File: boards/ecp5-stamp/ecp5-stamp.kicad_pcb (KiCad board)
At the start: 4 copper layers, 25 x 25 mm, 47 parts, among them J1 West, J2 South, J3 East, J4 North, J5 JTAG, SW1 ~RESET, SW2 ~USER, U1 W25Q128JVS, U2 MCP73831-2-OT, U3 ECP5UM_25_CSFBGA285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

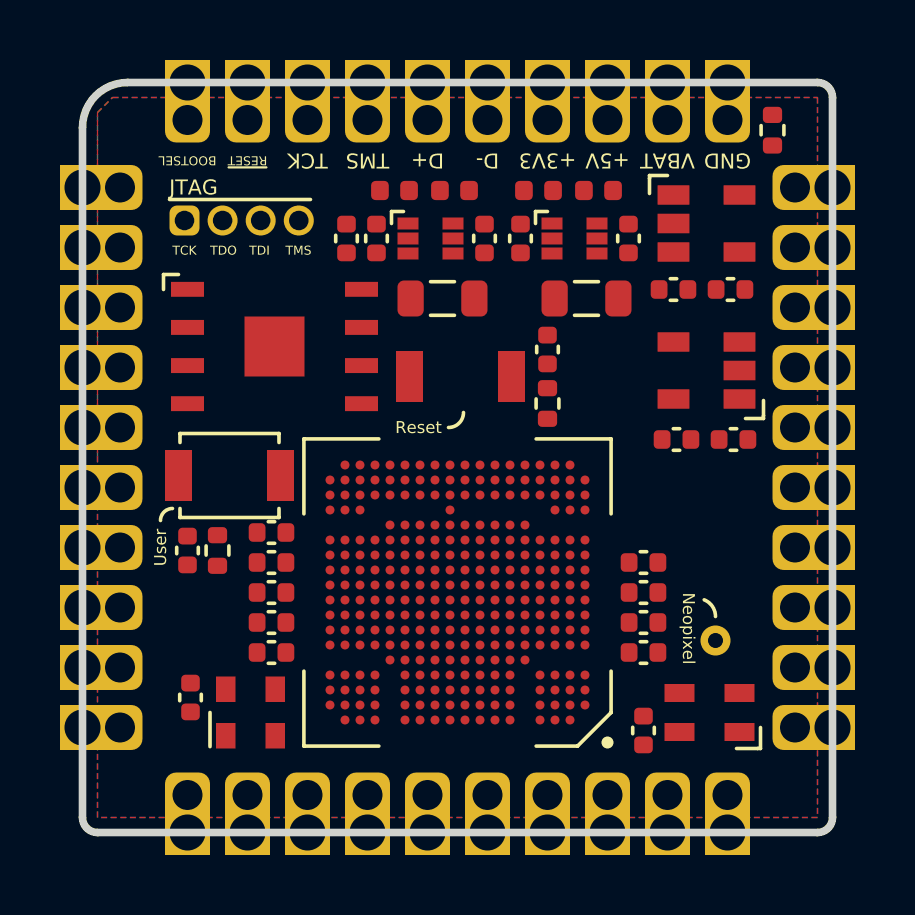
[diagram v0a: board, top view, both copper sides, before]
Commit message: Finished routing.
* Not sure what to do with BOOTSEL.
* Not sure if JTAG header is adequite.
* Not sure if should route dpairs equal length/together.
* etc.
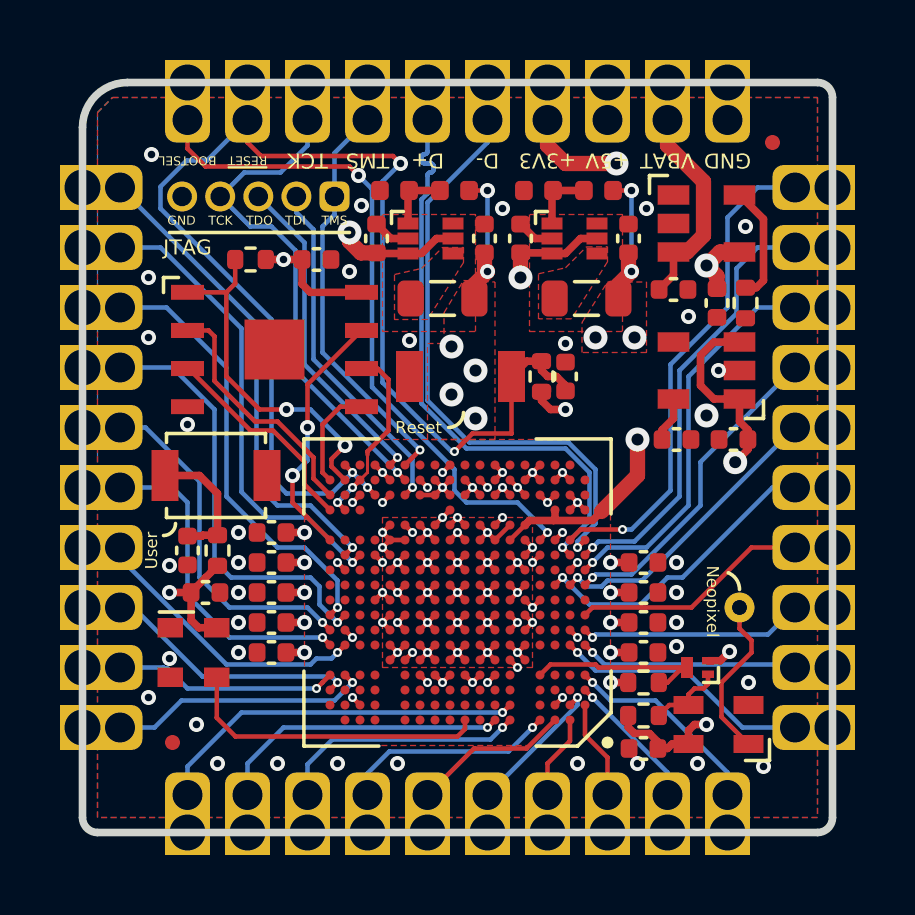
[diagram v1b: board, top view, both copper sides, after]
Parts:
- added FID1: Fiducial, Fiducial:Fiducial_0.5mm_Mask1mm, F.Cu at (25.0, 44.0)
- added FID2: Fiducial, Fiducial:Fiducial_0.5mm_Mask1mm, F.Cu at (45.0, 24.0)
- added Q1: DMN21D2UFB-7B, Package_DFN_QFN:Diodes_DFN1006-3, F.Cu at (42.5, 41.5)
- added R10: 4k7, Resistor_SMD:R_0402_1005Metric, F.Cu at (40.7, 43.1)
- added R8: 4k7, Resistor_SMD:R_0402_1005Metric, F.Cu at (27.6, 27.9)
- added R9: 4k7, Resistor_SMD:R_0402_1005Metric, F.Cu at (40.7, 42.0)
- J5: footprint Connector_PinHeader_1.27mm:PinHeader_1x04_P1.27mm_Vertical -> Connector_PinHeader_1.27mm:PinHeader_1x05_P1.27mm_Vertical
- moved R7 5.83 mm to (44.1, 29.4), turned to 270 degrees
- moved J5 5.06 mm to (30.4, 25.8), turned to 270 degrees
- moved C18 3.54 mm to (26.1, 39.0), turned to 0 degrees
- moved U4 2.76 mm to (25.7, 41.0), turned to 270 degrees
- moved TP1 1.36 mm to (43.9, 39.5)
- moved C17 1.22 mm to (29.8, 27.9), turned to 0 degrees
- moved C1 1.08 mm to (38.1, 31.8)
- moved C3 1.00 mm to (40.7, 39.0)
- moved C4 1.00 mm to (28.3, 39.0)
- moved C5 1.00 mm to (28.3, 40.0)
- moved C9 1.00 mm to (40.7, 40.0)
- moved R1 0.92 mm to (37.3, 31.8)
- moved C20 0.64 mm to (43.1, 29.4), turned to 270 degrees
- moved C21 0.60 mm to (40.7, 44.2), turned to 180 degrees
- moved D1 0.50 mm to (43.2, 43.4)
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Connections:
- net Net-(L1-Pad1) renamed /SW_1V1
- net Net-(L2-Pad1) renamed /SW_3V3
- C15 pad 1: +1V2 -> +1V1
- C3 pad 1: +1V2 -> +1V1
- C4 pad 1: +1V2 -> +1V1
- J5 pad 1: /JTAG_TCK -> /JTAG_TMS
- J5 pad 2: /JTAG_TDO -> /JTAG_TDI
- J5 pad 3: /JTAG_TDI -> /JTAG_TDO
- J5 pad 4: /JTAG_TMS -> /JTAG_TCK
- L1 pad 2: +1V2 -> +1V1
- R2 pad 1: +1V2 -> +1V1
- U3 pad A2: Net-(U3-PadA2) -> /GPIO_16
- U3 pad A3: Net-(U3-PadA3) -> /GPIO_14
- U3 pad A4: Net-(U3-PadA4) -> /GPIO_13
- U3 pad A6: Net-(U3-PadA6) -> /GPIO_12
- U3 pad A7: Net-(U3-PadA7) -> /GPIO_11
- U3 pad A9: Net-(U3-PadA9) -> /REF_CLK
- U3 pad B1: Net-(U3-PadB1) -> /GPIO_17
- U3 pad B2: Net-(U3-PadB2) -> /GPIO_15
- U3 pad B6: Net-(U3-PadB6) -> /GPIO_10
- U3 pad C1: Net-(U3-PadC1) -> /GPIO_18
- U3 pad C18: Net-(U3-PadC18) -> /GPIO_07
- U3 pad D1: Net-(U3-PadD1) -> /GPIO_19
- U3 pad D10: +1V2 -> +1V1
- U3 pad D11: +1V2 -> +1V1
- U3 pad D17: Net-(U3-PadD17) -> /GPIO_09
- U3 pad D18: Net-(U3-PadD18) -> /GPIO_08
- U3 pad D4: Net-(U3-PadD4) -> /NP_SDI_LV
- U3 pad D8: +1V2 -> +1V1
- U3 pad D9: +1V2 -> +1V1
- U3 pad F1: Net-(U3-PadF1) -> /GPIO_21
- U3 pad F17: Net-(U3-PadF17) -> /GPIO_06
- U3 pad F18: Net-(U3-PadF18) -> /GPIO_05
- U3 pad F2: Net-(U3-PadF2) -> /GPIO_20
- U3 pad G1: Net-(U3-PadG1) -> /GPIO_22
- U3 pad G18: Net-(U3-PadG18) -> /GPIO_04
- U3 pad H1: Net-(U3-PadH1) -> /GPIO_23
- U3 pad H17: Net-(U3-PadH17) -> /GPIO_03
- U3 pad H18: Net-(U3-PadH18) -> /GPIO_02
- U3 pad J14: +1V2 -> +1V1
- U3 pad J15: +1V2 -> +1V1
- U3 pad J4: +1V2 -> +1V1
- U3 pad J5: +1V2 -> +1V1
- U3 pad K1: Net-(U3-PadK1) -> /GPIO_26
- U3 pad K2: Net-(U3-PadK2) -> /GPIO_25
- U3 pad K3: Net-(U3-PadK3) -> /GPIO_24
- U3 pad L1: Net-(U3-PadL1) -> /GPIO_27
- U3 pad M1: Net-(U3-PadM1) -> /GPIO_28
- U3 pad M15: +1V2 -> +1V1
- U3 pad M16: Net-(U3-PadM16) -> /GPIO_01
- U3 pad M17: Net-(U3-PadM17) -> /GPIO_00
- U3 pad M2: Net-(U3-PadM2) -> /USB_D+
- U3 pad M4: +1V2 -> +1V1
- U3 pad N1: Net-(U3-PadN1) -> /USB_D-
- U3 pad N18: Net-(U3-PadN18) -> /FLASH_IO3
- U3 pad N2: Net-(U3-PadN2) -> /GPIO_29
- U3 pad N4: Net-(U3-PadN4) -> /BOOTSEL
- U3 pad P10: Net-(U3-PadP10) -> +1V1
- U3 pad P11: +1V2 -> +1V1
- U3 pad P7: +1V2 -> +1V1
- U3 pad P9: +1V2 -> +1V1
- U3 pad R10: Net-(U3-PadP10) -> +1V1
- U3 pad R17: Net-(U3-PadR17) -> /FLASH_SCK
- U3 pad R18: Net-(U3-PadR18) -> /FLASH_IO2
- U3 pad T14: Net-(U3-PadT14) -> +3V3
- U3 pad T15: Net-(U3-PadT15) -> /~RESET
- U3 pad T18: Net-(U3-PadT18) -> /FLASH_IO1
- U3 pad T5: Net-(U3-PadT5) -> +1V1
- U3 pad U12: Net-(U3-PadU12) -> +1V1
- U3 pad U14: Net-(U3-PadU14) -> GND
- U3 pad U16: Net-(U3-PadU16) -> /FLASH_SCK
- U3 pad U17: Net-(U3-PadU17) -> /FLASH_CS
- U3 pad U18: Net-(U3-PadU18) -> /FLASH_IO0
- U3 pad U6: Net-(U3-PadU6) -> +1V1
- U3 pad U8: Net-(U3-PadU8) -> +1V1
- U3 pad V15: Net-(U3-PadV15) -> GND
- U3 pad V17: Net-(U3-PadV17) -> /~RESET
- U4 pad 3: /OSC_12MHz -> /REF_CLK
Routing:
- net +5V: track 0.00 -> 54.2 mm, vias 0 -> 4
- net /~RESET: track 0.00 -> 43.5 mm, vias 0 -> 4
- net GND: track 0.00 -> 42.3 mm, vias 0 -> 76
- net +3V3: track 0.00 -> 41.1 mm, vias 0 -> 26
- net +2V5: track 0.00 -> 36.0 mm, vias 0 -> 4
- net /BOOTSEL: track 0.00 -> 22.9 mm, vias 0 -> 2
- net /USB_D-: track 0.00 -> 19.9 mm, vias 0 -> 1
- net /USB_D+: track 0.00 -> 19.8 mm, vias 0 -> 1
- net +1V1: track 0.00 -> 17.9 mm, vias 0 -> 20
- net /JTAG_TCK: track 0.00 -> 16.9 mm, vias 0 -> 1
- net /GPIO_29: track 0.00 -> 16.6 mm, vias 0 -> 1
- net /GPIO_00: track 0.00 -> 16.2 mm, vias 0 -> 1
- net /GPIO_02: track 0.00 -> 15.8 mm, vias 0 -> 1
- net /GPIO_01: track 0.00 -> 15.6 mm, vias 0 -> 1
- net /GPIO_28: track 0.00 -> 14.6 mm, vias 0 -> 1
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- added copper zone on F.Cu, net +1V1
- added copper zone on In1.Cu, net +1V1
- added copper zone on F.Cu, net +3V3
- added copper zone on In1.Cu, net +3V3
- added copper zone on F.Cu, net /SW_1V1
- added copper zone on F.Cu, net /SW_3V3
- added copper zone on In2.Cu, net GND
- removed copper zone on In2.Cu, net +3V3
- removed copper zone on In1.Cu, net GND
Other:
- net class Default: clearance 0.2 -> 0.01
- rule trace_clearance: 0.2 -> 0.01
- board text added: "0"
- board text added: "10"
- board text added: "20"

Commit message: Added 2v5 decoupling caps.
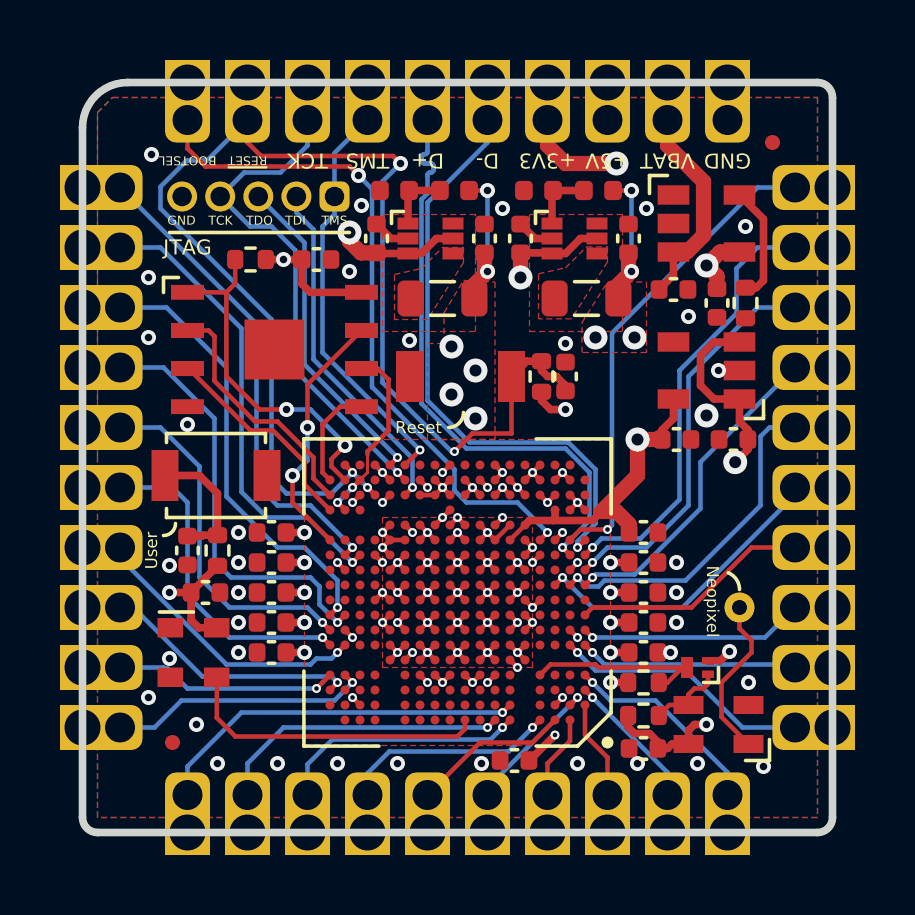
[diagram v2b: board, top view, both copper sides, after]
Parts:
- added C23: 0.1u, Capacitor_SMD:C_0402_1005Metric, F.Cu at (36.4, 44.6)
- added C24: 0.1u, Capacitor_SMD:C_0402_1005Metric, F.Cu at (40.7, 37.0)
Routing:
- net +2V5: track 36.0 -> 39.6 mm, vias 4 -> 5
- net /GPIO_25: track 9.92 -> 11.3 mm
- net GND: vias 76 -> 77

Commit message: Tweaked and fixed signal and power traces.
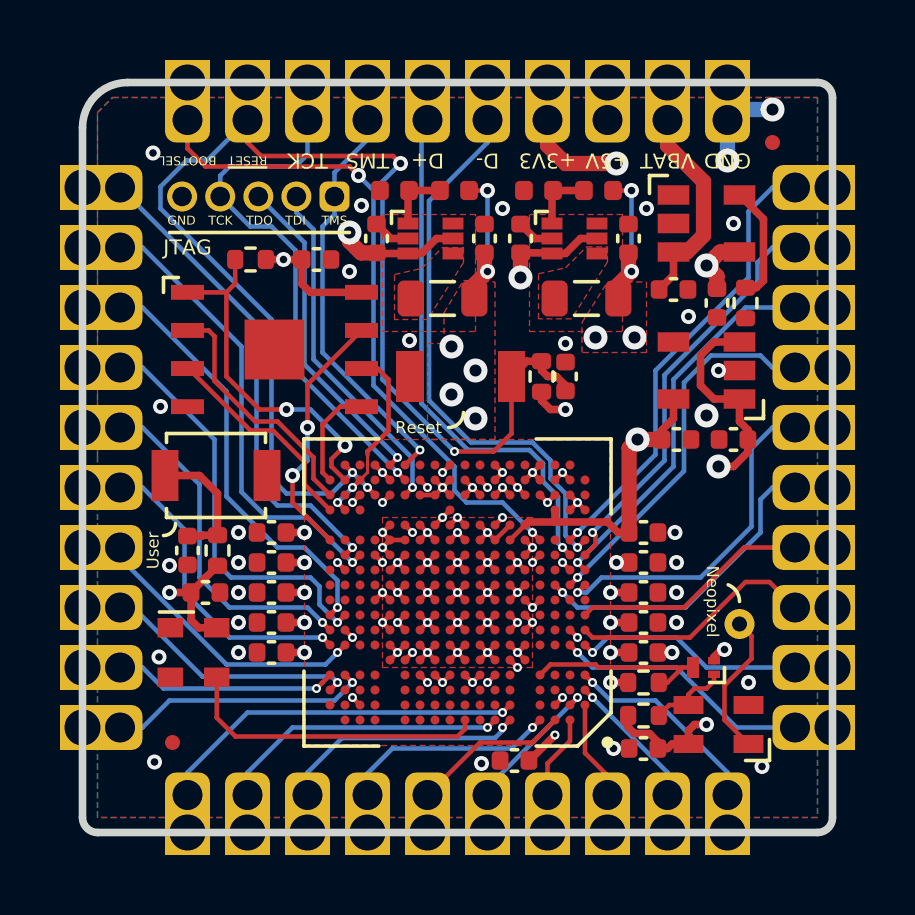
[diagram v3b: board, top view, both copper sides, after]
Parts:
- moved TP1 0.55 mm to (43.9, 40.0)
- moved Q1 0.20 mm to (42.7, 41.5)
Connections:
- U3 pad K1: /GPIO_26 -> /GPIO_25
- U3 pad K2: /GPIO_25 -> /GPIO_26
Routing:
- net +1V1: track 17.9 -> 26.9 mm
- net GND: track 42.3 -> 45.3 mm, vias 77 -> 71
- net /USB_D+: track 19.8 -> 17.8 mm
- net /GPIO_26: track 10.9 -> 12.8 mm
- net /USB_D-: track 19.9 -> 18.7 mm
- net /GPIO_28: track 14.6 -> 13.7 mm
- net /GPIO_29: track 16.1 -> 15.3 mm
- net /GPIO_22: track 7.52 -> 8.22 mm, vias 1 -> 0
- net /NP_SDO: track 5.50 -> 4.87 mm
- net /GPIO_05: track 11.0 -> 10.4 mm
- net /JTAG_TCK: track 16.9 -> 17.5 mm
- net /GPIO_21: track 7.31 -> 7.87 mm
- net /BOOTSEL: track 22.9 -> 22.4 mm
- net Net-(U3-PadN3): track 0.35 -> 0.00 mm, vias 1 -> 0
